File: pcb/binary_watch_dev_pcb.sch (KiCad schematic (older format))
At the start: 67 parts, among them K1 PWR_SELECT, M1 MNT, M2 MNT, M3 MNT, M4 MNT, P1 ISP, P2 USB-MICRO-B, P3 LED_ISENSE, P7 MCU_ISENSE, P8 TST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

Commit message: Add new dev pcb files from nightly build of kicad
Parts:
- added NET? (x4): NET_CONN, symbol NET_CONN
- C6, C7: footprint Capacitors_SMD:C_0603_HandSoldering -> Capacitors_SMD:C_0402
- SW1A1, SW2A1: Manufacturer P/N (none) -> EVQ-P7C01P; Vendor P/N (none) -> P16765CT-ND
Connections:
- wire segments 269 -> 204
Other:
- moved on the sheet: C1, C8

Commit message: Finish dev schematic and layout, create gerbers to send to manufacture
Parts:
- NET1, NET2, NET3, NET4: renamed from NET?; footprint (none) -> _ Custom Lib:NET_CONN
- SW1A1, SW2A1: footprint (none) -> _ Custom Lib:EVQ-P7C01P
- U3: footprint SMD_Packages:SOT-223 -> _ Custom Lib:SOT-223
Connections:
- wire segments 204 -> 267
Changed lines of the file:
@@
 F 0 "SW2A1" H 10500 5760 50  0000 C CNN
 F 1 "BUTTON_2" H 10350 5570 50  0000 C CNN
-F 2 "" H 10350 5650 60  0001 C CNN
+F 2 "_ Custom Lib:EVQ-P7C01P" H 10350 5650 60  0001 C CNN
 F 3 "~" H 10350 5650 60  0000 C CNN
 F 4 "EVQ-P7C01P" H 10350 5650 60  0001 C CNN "Manufacturer P/N"
@@
 $EndComp
 $Comp
-L NCP1117ST33T3G U3
-U 1 1 5430EF90
-P 4250 4250
-F 0 "U3" H 4250 4500 40  0000 C CNN
-F 1 "NCP1117ST33T3G" H 4250 4450 40  0000 C CNN
-F 2 "SMD_Packages:SOT-223" H 4250 4250 60  0001 C CNN
-F 3 "" H 4250 4250 60  0000 C CNN
-F 4 "NCP1117STAT3G" H 4250 4250 60  0001 C CNN "Manufacturer P/N"
-F 5 "NCP1117STAT3GOSCT-ND" H 4250 4250 60  0001 C CNN "Vendor P/N"
-	1    4250 4250
-	1    0    0    -1
-$EndComp
-$Comp
 L R R17
 U 1 1 5430F1C1
@@
 	10650 5200 10800 5200
 Wire Wire Line
-	10800 4900 10800 6050
+	10800 4900 10800 5200
+Wire Wire Line
+	10800 5200 10800 5650
+Wire Wire Line
+	10800 5650 10800 5950
+Wire Wire Line
+	10800 5950 10800 6050
 Wire Wire Line
 	10800 5650 10650 5650
@@
 	9700 4450 9700 4550
 Wire Wire Line
-	9500 4350 9500 4550
-Wire Wire Line
-	9950 5300 9950 5950
+	9500 4350 9500 4450
+Wire Wire Line
+	9500 4450 9500 4550
+Wire Wire Line
+	9950 5300 9950 5650
+Wire Wire Line
+	9950 5650 9950 5950
 Wire Wire Line
 	9500 5050 9500 5300
@@
 	3950 1900 4200 1900
 Wire Wire Line
-	2100 1400 4200 1400
+	2100 1400 2150 1400
+Wire Wire Line
+	2150 1400 3200 1400
+Wire Wire Line
+	3200 1400 3450 1400
+Wire Wire Line
+	3450 1400 3700 1400
+Wire Wire Line
+	3700 1400 4100 1400
+Wire Wire Line
+	4100 1400 4200 1400
 Wire Wire Line
 	4200 1300 4100 1300
 Wire Wire Line
-	4100 1300 4100 1600
+	4100 1300 4100 1400
+Wire Wire Line
+	4100 1400 4100 1600
 Connection ~ 4100 1400
 Wire Wire Line
@@
 	4100 3600 4200 3600
 Wire Wire Line
-	4100 3400 4100 3600
+	4100 3400 4100 3500
+Wire Wire Line
+	4100 3500 4100 3600
 Connection ~ 4100 3400
 Wire Wire Line
@@
 Connection ~ 3700 3400
 Wire Wire Line
-	900  2800 900  3500
+	900  2800 900  3400
+Wire Wire Line
+	900  3400 900  3500
 Connection ~ 3450 3400
 Wire Wire Line
@@
 Connection ~ 900  3400
 Wire Wire Line
-	6350 3700 6350 4150
+	6350 3700 6350 4050
+Wire Wire Line
+	6350 4050 6350 4150
 Wire Wire Line
 	6350 4050 6450 4050
@@
 	6100 1900 7150 1900
 Wire Wire Line
-	7150 1900 7150 4150
+	7150 1900 7150 4050
+Wire Wire Line
+	7150 4050 7150 4150
 Wire Wire Line
 	6350 4550 6350 4650
@@
 	7050 3700 6350 3700
 Wire Wire Line
-	9150 5300 9950 5300
+	9150 5300 9500 5300
+Wire Wire Line
+	9500 5300 9950 5300
 Wire Wire Line
 	6100 3200 8500 3200
@@
 	9450 5950 9550 5950
 Wire Wire Line
-	9550 5950 9550 6350
+	9550 5950 9550 6250
+Wire Wire Line
+	9550 6250 9550 6350
 Wire Wire Line
 	9450 5750 9550 5750
@@
 	6100 2150 6550 2150
 Wire Wire Line
-	9150 5200 10050 5200
+	9150 5200 9700 5200
+Wire Wire Line
+	9700 5200 9950 5200
+Wire Wire Line
+	9950 5200 10050 5200
 Wire Wire Line
 	6550 1500 6100 1500
@@
 	6100 1400 6550 1400
 Wire Wire Line
-	10500 2650 10500 3950
+	10500 2650 10500 2750
+Wire Wire Line
+	10500 2750 10500 3050
+Wire Wire Line
+	10500 3050 10500 3350
+Wire Wire Line
+	10500 3350 10500 3650
+Wire Wire Line
+	10500 3650 10500 3950
 Wire Wire Line
 	10500 3950 10400 3950
@@
 	10500 2300 10400 2300
 Wire Wire Line
-	10500 700  10500 2300
+	10500 700  10500 800
+Wire Wire Line
+	10500 800  10500 1100
+Wire Wire Line
+	10500 1100 10500 1400
+Wire Wire Line
+	10500 1400 10500 1700
+Wire Wire Line
+	10500 1700 10500 2000
+Wire Wire Line
+	10500 2000 10500 2300
 Wire Wire Line
 	10400 800  10500 800
@@
 	9900 2300 10000 2300
 Wire Wire Line
-	900  3400 4200 3400
+	900  3400 1200 3400
+Wire Wire Line
+	1200 3400 1450 3400
+Wire Wire Line
+	1450 3400 2950 3400
+Wire Wire Line
+	2950 3400 3200 3400
+Wire Wire Line
+	3200 3400 3450 3400
+Wire Wire Line
+	3450 3400 3700 3400
+Wire Wire Line
+	3700 3400 3950 3400
+Wire Wire Line
+	3950 3400 4100 3400
+Wire Wire Line
+	4100 3400 4200 3400
 Wire Wire Line
 	9500 4450 9700 4450
 Connection ~ 9500 4450
 Wire Wire Line
-	8150 5850 8150 6250
+	8150 5850 8150 5950
+Wire Wire Line
+	8150 5950 8150 6250
 Wire Wire Line
 	8150 5350 8150 5250
@@
 	4100 1600 4200 1600
 Wire Wire Line
-	3450 1300 3450 2350
+	3450 1300 3450 1400
+Wire Wire Line
+	3450 1400 3450 2350
 Connection ~ 3450 1400
 Wire Wire Line
-	2950 1750 2950 2350
+	2950 1750 2950 1850
+Wire Wire Line
+	2950 1850 2950 2350
 Connection ~ 2950 1850
 Connection ~ 3200 1400
 Wire Wire Line
-	1450 1300 1450 2200
+	1450 1300 1450 1400
+Wire Wire Line
+	1450 1400 1450 1850
+Wire Wire Line
+	1450 1850 1450 2200
 Connection ~ 1450 1400
 Wire Wire Line
@@
 	1000 1000 1000 1400
 Wire Wire Line
-	1000 1400 1600 1400
+	1000 1400 1200 1400
+Wire Wire Line
+	1200 1400 1450 1400
+Wire Wire Line
+	1450 1400 1550 1400
+Wire Wire Line
+	1550 1400 1600 1400
 Wire Wire Line
 	1100 1000 1100 1100
@@
 	900  4800 1000 4800
 Wire Wire Line
-	900  4200 900  4900
+	900  4200 900  4350
+Wire Wire Line
+	900  4350 900  4650
+Wire Wire Line
+	900  4650 900  4800
+Wire Wire Line
+	900  4800 900  4900
 Wire Wire Line
 	1000 4200 900  4200
@@
 Connection ~ 900  4350
 Wire Wire Line
-	3200 4200 3850 4200
-Wire Wire Line
-	4650 4200 5650 4200
-Wire Wire Line
-	4250 4500 4250 4950
+	3200 4200 3700 4200
+Wire Wire Line
+	3700 4200 3800 4200
+Wire Wire Line
+	3800 4200 3850 4200
+Wire Wire Line
+	4800 4200 5300 4200
+Wire Wire Line
+	5300 4200 5650 4200
+Wire Wire Line
+	4250 4500 4250 4600
+Wire Wire Line
+	4250 4600 4250 4850
+Wire Wire Line
+	4250 4850 4250 4950
 Wire Wire Line
 	4250 4850 4800 4850
 Wire Wire Line
-	4800 4800 4800 4900
+	4800 4800 4800 4850
+Wire Wire Line
+	4800 4850 4800 4900
 Connection ~ 4800 4850
 Wire Wire Line
@@
 	5300 5050 5300 5500
 Wire Wire Line
-	2100 4200 2700 4200
+	2100 4200 2150 4200
+Wire Wire Line
+	2150 4200 2700 4200
 Wire Wire Line
 	7850 1350 7850 1450
@@
 	8100 4800 8100 4900
 Wire Wire Line
-	5100 6000 5100 6500
+	5100 6000 5100 6100
+Wire Wire Line
+	5100 6100 5100 6500
 Wire Wire Line
 	5400 6100 5100 6100
 Connection ~ 5100 6100
 Wire Wire Line
-	5100 6900 5100 7100
+	5100 6900 5100 7000
+Wire Wire Line
+	5100 7000 5100 7100
 Wire Wire Line
 	5100 7000 5300 7000
@@
 	5400 6300 4350 6300
 Wire Wire Line
-	6400 6050 6400 7100
+	6400 6050 6400 6450
+Wire Wire Line
+	6400 6450 6400 7100
 Wire Wire Line
 	6400 6450 6300 6450
@@
 LED_SNSI_P
 Wire Wire Line
-	1450 1850 1600 1850
-Wire Wire Line
-	2100 1850 3200 1850
+	1450 1850 1550 1850
+Wire Wire Line
+	1550 1850 1600 1850
+Wire Wire Line
+	2100 1850 2150 1850
+Wire Wire Line
+	2150 1850 2950 1850
+Wire Wire Line
+	2950 1850 3200 1850
 Wire Wire Line
 	2150 1400 2150 1500
@@
 $EndComp
 Wire Wire Line
-	1500 6000 1500 6500
+	1500 6000 1500 6100
+Wire Wire Line
+	1500 6100 1500 6500
 Wire Wire Line
 	1800 6100 1500 6100
 Connection ~ 1500 6100
 Wire Wire Line
-	1500 6900 1500 7100
+	1500 6900 1500 7000
+Wire Wire Line
+	1500 7000 1500 7100
 Wire Wire Line
 	1500 7000 1700 7000
@@
 	1800 6300 750  6300
 Wire Wire Line
-	2800 6050 2800 7100
+	2800 6050 2800 6450
+Wire Wire Line
+	2800 6450 2800 7100
 Wire Wire Line
 	2800 6450 2700 6450
@@
 $EndComp
 Wire Wire Line
-	3200 1800 3200 2350
+	3200 1800 3200 1850
+Wire Wire Line
+	3200 1850 3200 2350
 $Comp
 L PWR_FLAG #FLG033
@@
 Wire Wire Line
 	8750 6250 8850 6250
-Wire Wire Line
-	4450 4500 4450 4550
-Wire Wire Line
-	4450 4550 4700 4550
-Wire Wire Line
-	4700 4550 4700 4200
-Connection ~ 4700 4200
 $Comp
 L SW_PUSH SW1A1
@@
 F 0 "SW1A1" H 10500 5010 50  0000 C CNN
 F 1 "BUTTON_1" H 10350 4820 50  0000 C CNN
-F 2 "" H 10350 4900 60  0001 C CNN
+F 2 "_ Custom Lib:EVQ-P7C01P" H 10350 4900 60  0001 C CNN
 F 3 "~" H 10350 4900 60  0000 C CNN
 F 4 "EVQ-P7C01P" H 10350 4900 60  0001 C CNN "Manufacturer P/N"
@@
 Connection ~ 3200 1850
 $Comp
-L NET_CONN NET?
+L NET_CONN NET1
 U 1 1 543B4750
 P 2300 1500
-F 0 "NET?" H 2300 1600 60  0001 C CNN
+F 0 "NET1" H 2300 1600 60  0001 C CNN
 F 1 "NET_CONN" H 2300 1400 60  0001 C CNN
-F 2 "" H 2300 1500 60  0000 C CNN
+F 2 "_ Custom Lib:NET_CONN" H 2300 1500 60  0001 C CNN
 F 3 "" H 2300 1500 60  0000 C CNN
 	1    2300 1500
@@
 $EndComp
 $Comp
-L NET_CONN NET?
+L NET_CONN NET2
 U 1 1 543B5161
 P 2300 1600
-F 0 "NET?" H 2300 1700 60  0001 C CNN
+F 0 "NET2" H 2300 1700 60  0001 C CNN
 F 1 "NET_CONN" H 2300 1500 60  0001 C CNN
-F 2 "" H 2300 1600 60  0000 C CNN
+F 2 "_ Custom Lib:NET_CONN" H 2300 1600 60  0001 C CNN
 F 3 "" H 2300 1600 60  0000 C CNN
 	1    2300 1600
@@
 	2400 1600 2950 1600
 $Comp
-L NET_CONN NET?
+L NET_CONN NET3
 U 1 1 543B6469
 P 2300 1950
-F 0 "NET?" H 2300 2050 60  0001 C CNN
+F 0 "NET3" H 2300 2050 60  0001 C CNN
 F 1 "NET_CONN" H 2300 1850 60  0001 C CNN
-F 2 "" H 2300 1950 60  0000 C CNN
+F 2 "_ Custom Lib:NET_CONN" H 2300 1950 60  0001 C CNN
 F 3 "" H 2300 1950 60  0000 C CNN
 	1    2300 1950
@@
 $EndComp
 $Comp
-L NET_CONN NET?
+L NET_CONN NET4
 U 1 1 543B64B7
 P 2300 2050
-F 0 "NET?" H 2300 2150 60  0001 C CNN
+F 0 "NET4" H 2300 2150 60  0001 C CNN
 F 1 "NET_CONN" H 2300 1950 60  0001 C CNN
-F 2 "" H 2300 2050 60  0000 C CNN
+F 2 "_ Custom Lib:NET_CONN" H 2300 2050 60  0001 C CNN
 F 3 "" H 2300 2050 60  0000 C CNN
 	1    2300 2050
@@
 Wire Wire Line
 	2400 2050 2900 2050
+$Comp
+L NCP1117ST33T3G U3
+U 1 1 5430EF90
+P 4250 4250
+F 0 "U3" H 4250 4500 40  0000 C CNN
+F 1 "NCP1117ST33T3G" H 4250 4450 40  0000 C CNN
+F 2 "_ Custom Lib:SOT-223" H 4250 4250 60  0001 C CNN
+F 3 "" H 4250 4250 60  0000 C CNN
+F 4 "NCP1117STAT3G" H 4250 4250 60  0001 C CNN "Manufacturer P/N"
+F 5 "NCP1117STAT3GOSCT-ND" H 4250 4250 60  0001 C CNN "Vendor P/N"
+	1    4250 4250
+	1    0    0    -1
+$EndComp
+Wire Wire Line
+	4700 4200 4800 4200
+Wire Wire Line
+	4650 4200 4700 4200
 $EndSCHEMATC

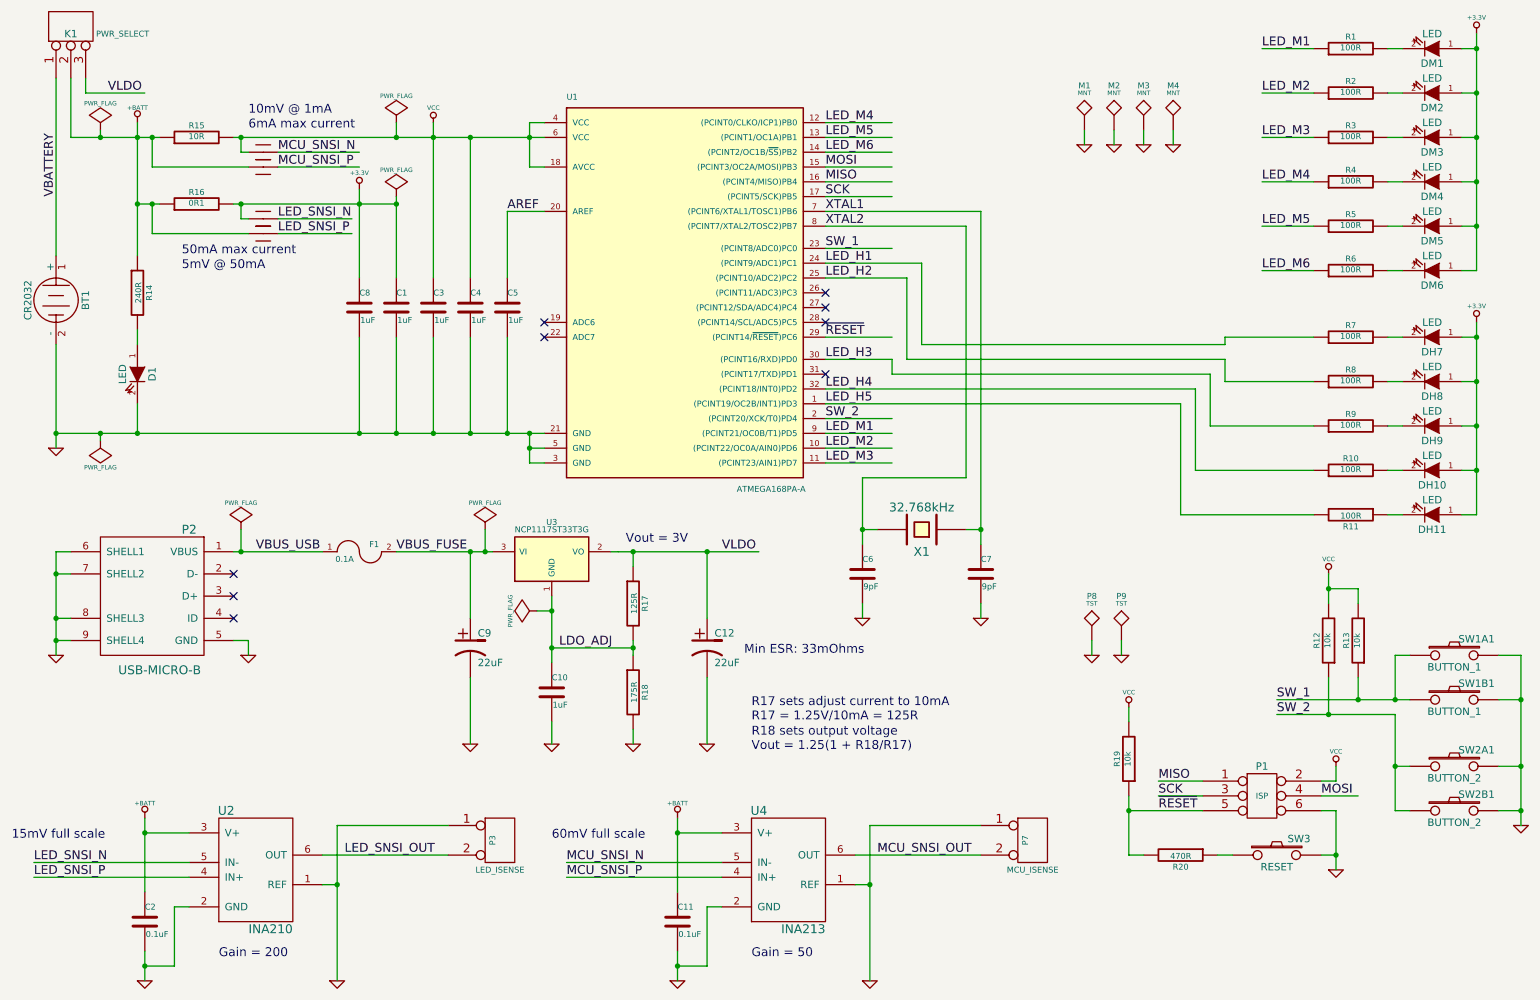
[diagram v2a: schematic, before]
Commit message: Add makefile, get first running code to PWM LEDs
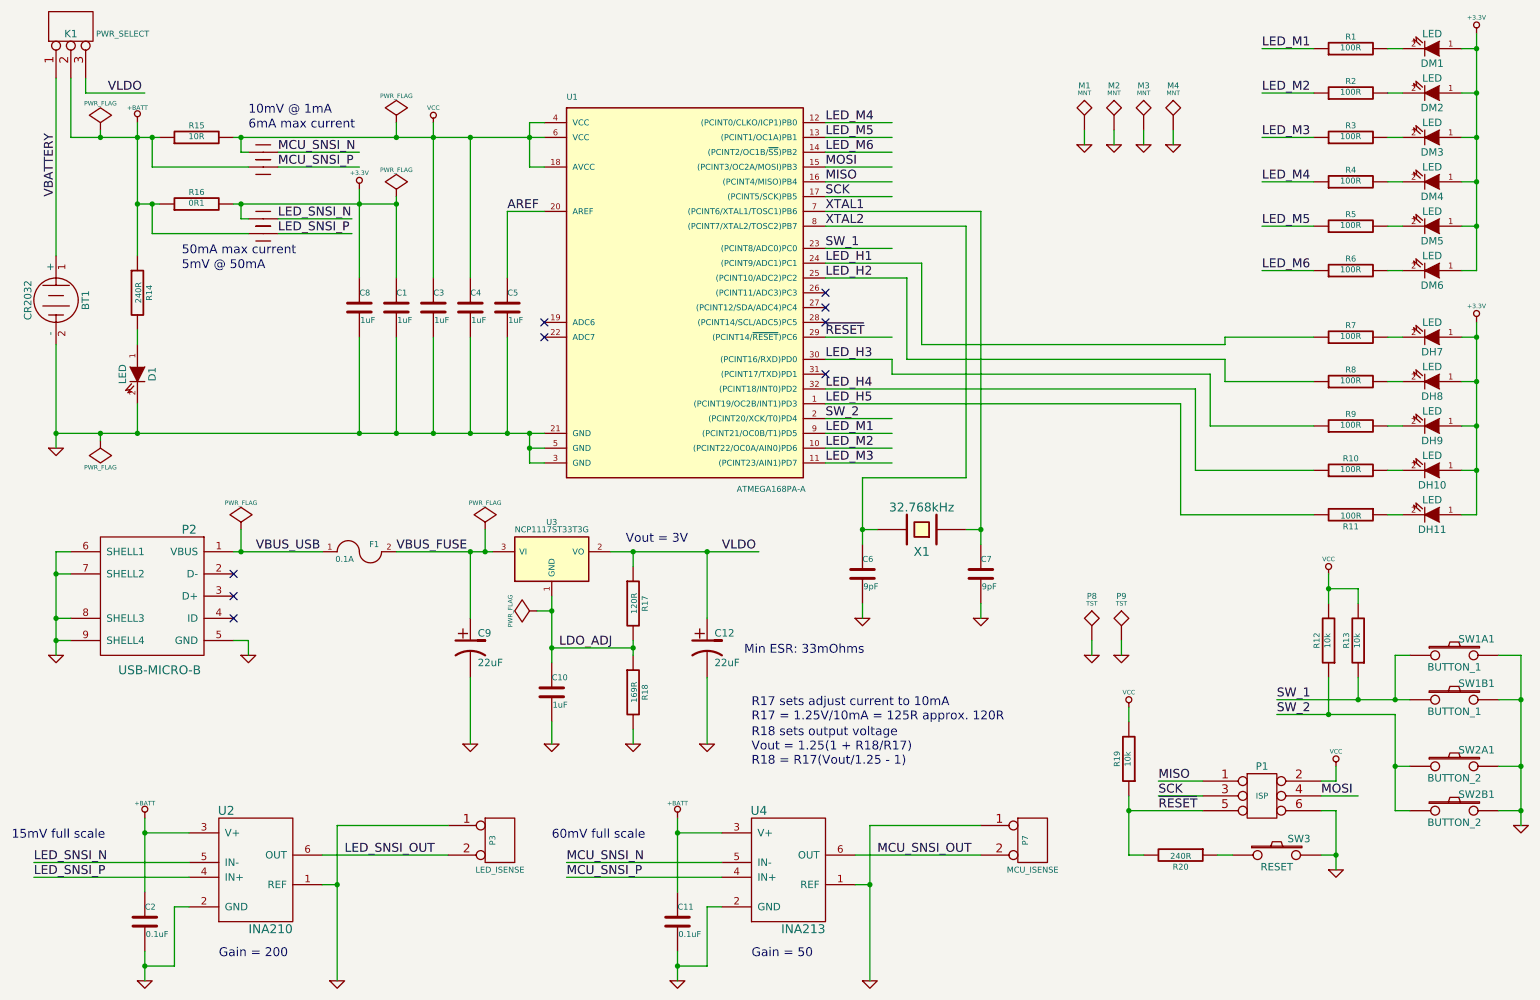
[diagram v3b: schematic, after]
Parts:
- C1, C10, C11, C2, C3, C4, C5, C8: Manufacturer P/N (none) -> LMK107B7105KA-T; Vendor P/N (none) -> 587-1242-1-ND
- C12, C9: Manufacturer P/N (none) -> EDK226M016A9BAA; Vendor P/N (none) -> 399-11437-1-ND
- C6, C7: Manufacturer P/N (none) -> GRM1555C1H9R0BA01D; Vendor P/N (none) -> 490-6257-1-ND
- K1: Manufacturer P/N (none) -> M20-9990345; Vendor P/N (none) -> 952-2263-ND
- R17: value 125R -> 120R; Vendor P/N (none) -> P120HCT-ND
- R18: value 175R -> 169R; Vendor P/N (none) -> P169HCT-ND
- R20: value 470R -> 240R
- U2: Manufacturer P/N (none) -> INA210AIDCKT; Vendor P/N (none) -> 296-23420-1-ND
- U4: Manufacturer P/N (none) -> INA213AIDCKR; Vendor P/N (none) -> 296-26072-1-ND
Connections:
- wire segments 267 -> 201
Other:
- note added: "R17 sets adjust current to 10mA\nR17 = 1.25V/10mA = 125R approx. 120R"
- note added: "R18 sets output voltage\nVout = 1.25(1 + R18/R17)\nR18 = R17(Vout/1.25 - 1)"
- note removed: "R17 sets adjust current to 10mA\nR17 = 1.25V/10mA = 125R"
- note removed: "R18 sets output voltage\nVout = 1.25(1 + R18/R17)"

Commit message: Gen fab outputs, pdfs, and finish final routing.
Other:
- note added: "I_LEDS = V / 20"
- note added: "I_MCU = V / 500"
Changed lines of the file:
@@
 	1    0    0    -1
 $EndComp
+Text Notes 6600 6500 0    60   ~ 0
+I_MCU = V / 500
+Text Notes 3100 6550 0    60   ~ 0
+I_LEDS = V / 20
 $EndSCHEMATC
